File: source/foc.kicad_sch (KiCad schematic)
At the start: 22 parts, among them J1 Conn_01x03, J2 Conn_01x04_Male, J3 Conn_01x05, J4 Conn_01x12, SW1 SW_DPDT_x2, U1 TJA1050T/CM,118

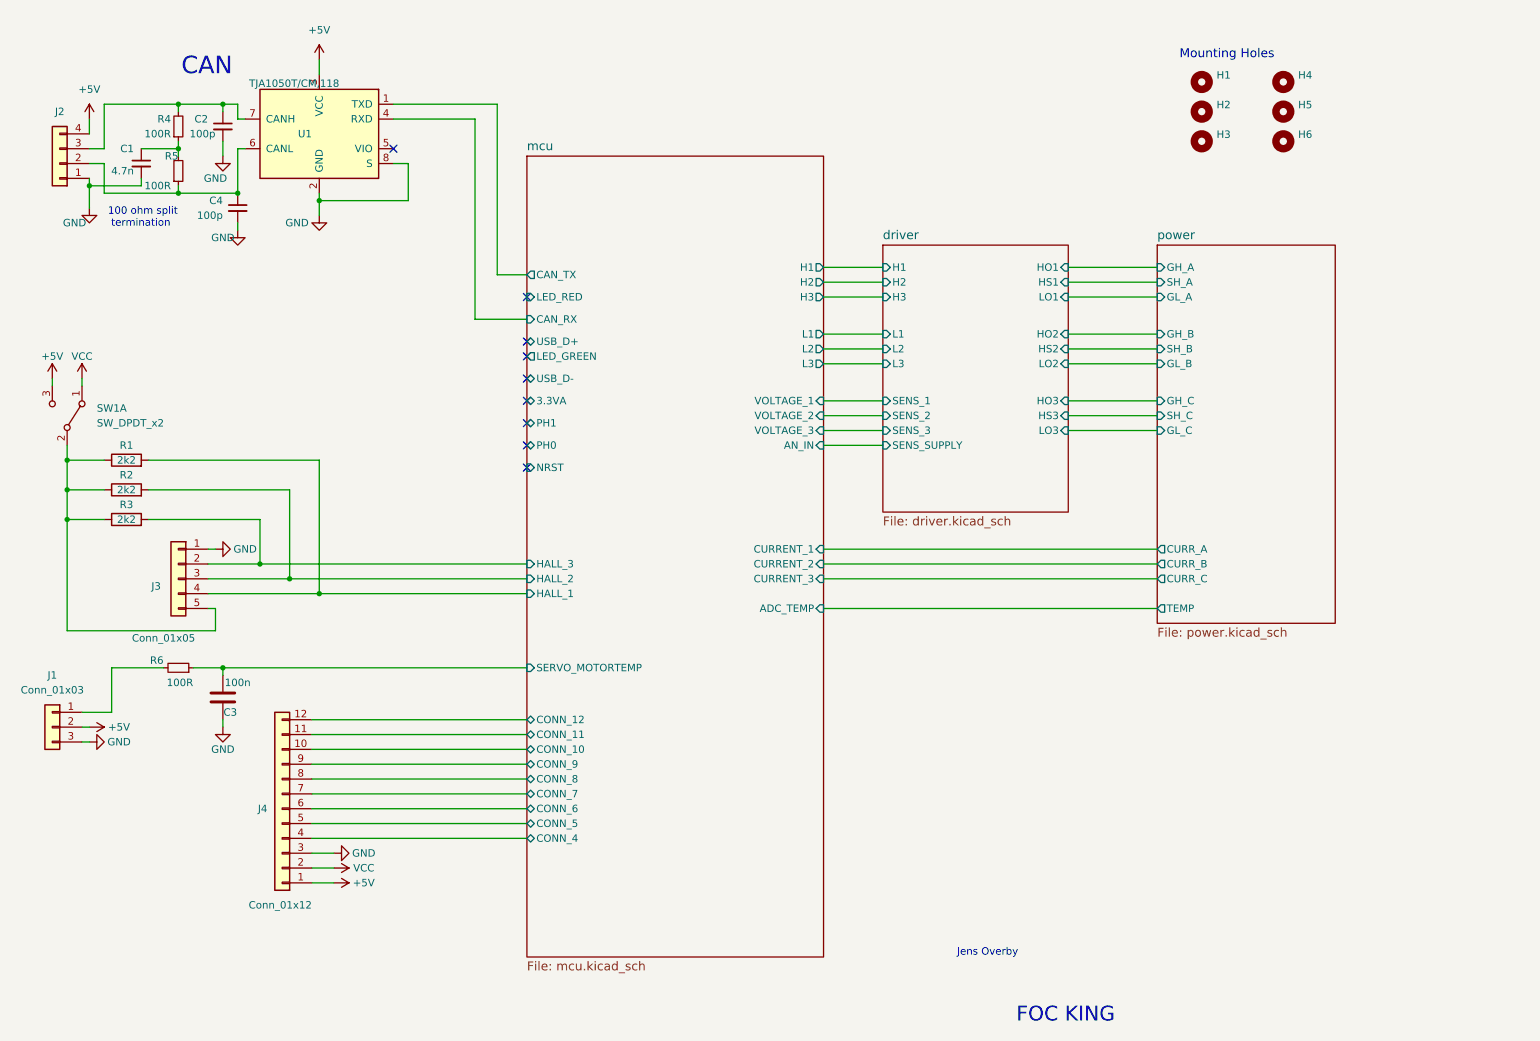
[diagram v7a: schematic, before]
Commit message: JLCPCB order with separate power supply
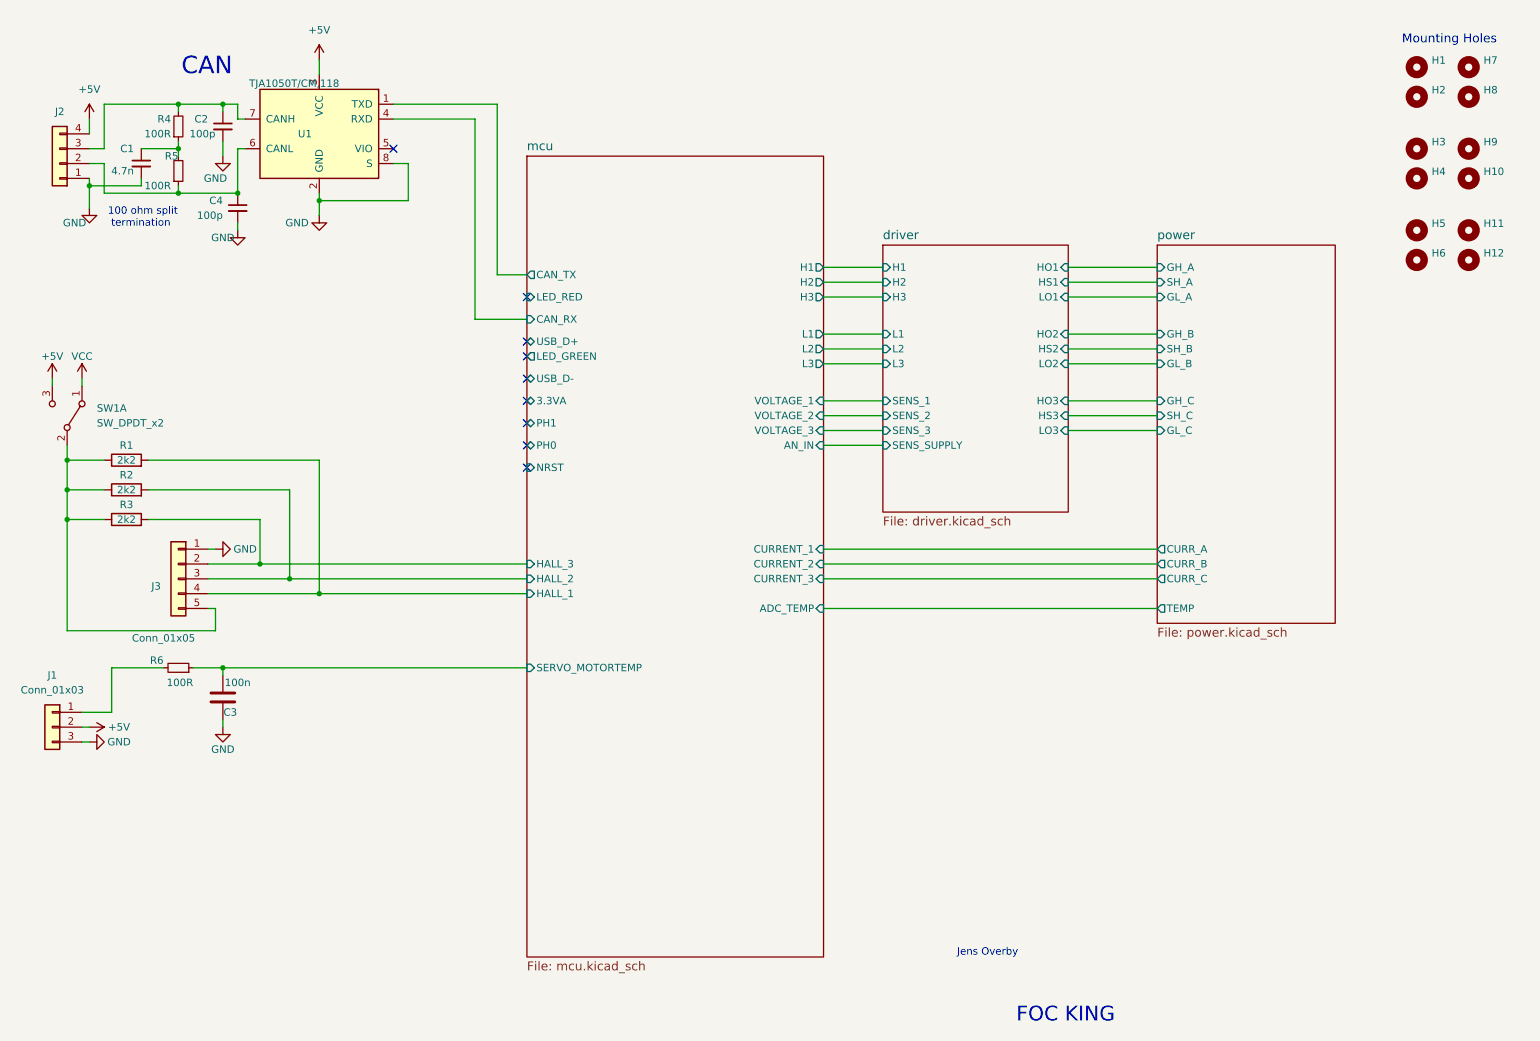
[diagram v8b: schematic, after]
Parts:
- removed J4: Conn_01x12, Connector_JST:JST_PH_B12B-PH-K_1x12_P2.00mm_Vertical, symbol Connector_Generic:Conn_01x12
- added H11, H12, H2, H5, H6, H8: MountingHole, MountingHole:MountingHole_3.2mm_M3, symbol Mechanical:MountingHole
- renumbered H5 to H1, H1 to H10, H2 to H4, H6 to H7, H4 to H9
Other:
- sheet mcu ports: added none; removed CONN_10, CONN_11, CONN_12, CONN_4, CONN_5, CONN_6, CONN_7, CONN_8, CONN_9
- moved on the sheet: H1, H10, H3, H4, H7, H9
